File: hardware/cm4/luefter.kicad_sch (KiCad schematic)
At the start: 6 parts, among them J15 Lüfter 5 V, Q11 AO3400A

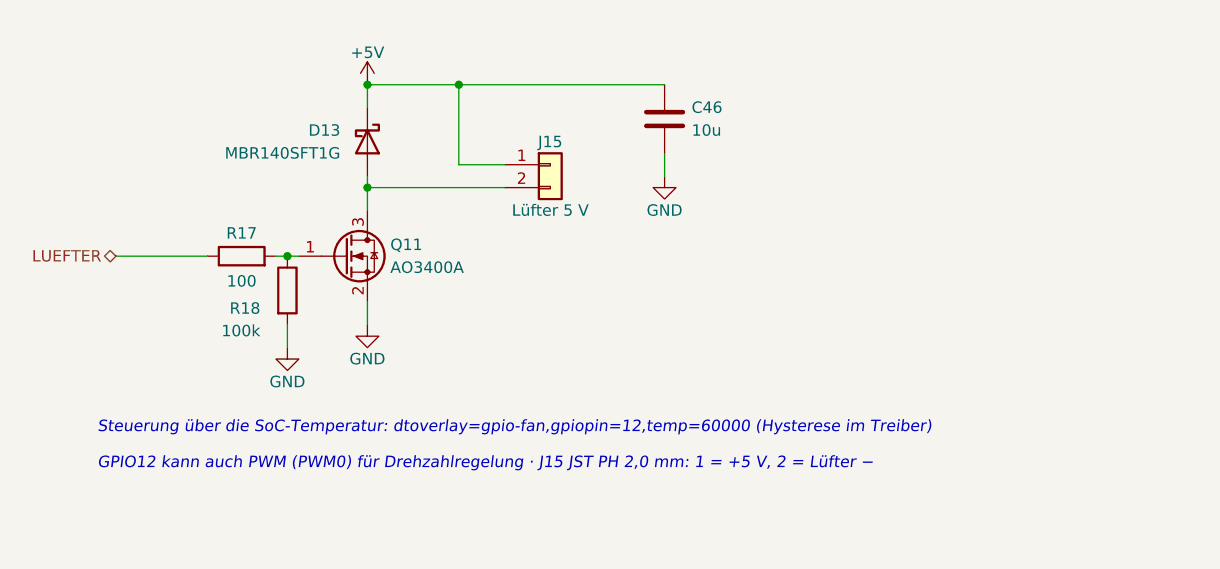
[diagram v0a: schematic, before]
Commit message: Schaltplan: Hinweise als Textkästen (KiCad bricht um); Texte werden in den Generator zurückgeführt
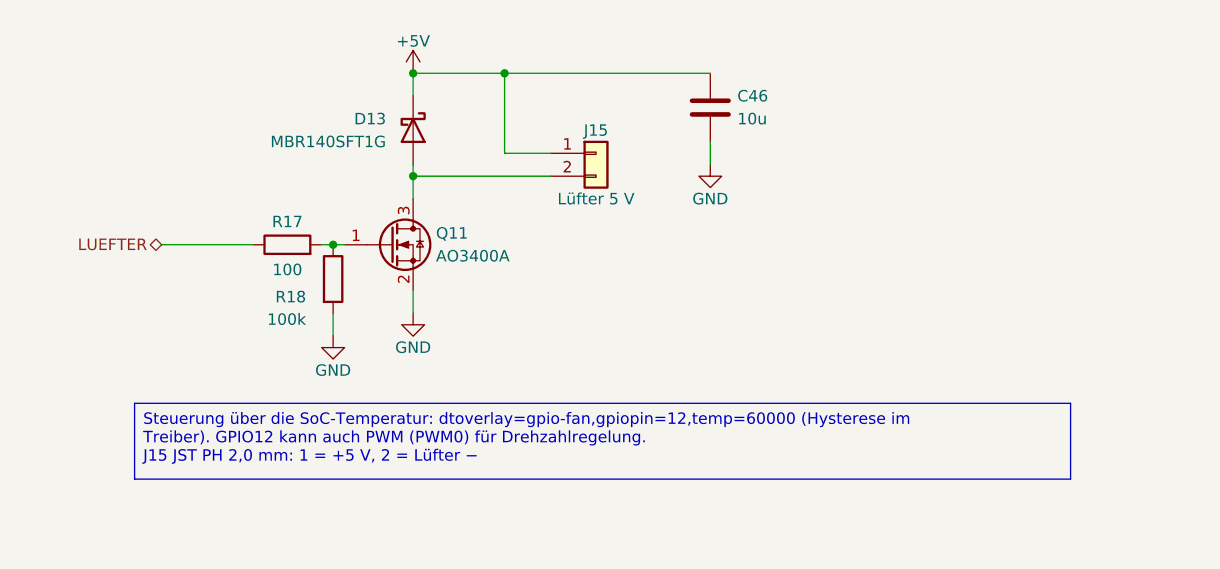
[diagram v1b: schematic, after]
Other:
- note removed: "GPIO12 kann auch PWM (PWM0) für Drehzahlregelung · J15 JST PH 2,0 mm: 1 = +5 V, 2 = Lüfter −"
- note removed: "Steuerung über die SoC-Temperatur: dtoverlay=gpio-fan,gpiopin=12,temp=60000 (Hysterese im Treiber)"
- moved on the sheet: C46, D13, J15, Q11, R17, R18

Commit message: CM4-Schaltplan: Handänderungen übernommen (Handlage für 8 Blätter, 2 Texte zurückgeführt); Kastenhöhen aus gemessenen Zeichenbreiten
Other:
- moved on the sheet: C46, D13, J15, Q11, R17, R18
